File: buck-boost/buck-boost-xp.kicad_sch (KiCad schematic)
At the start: 0 parts

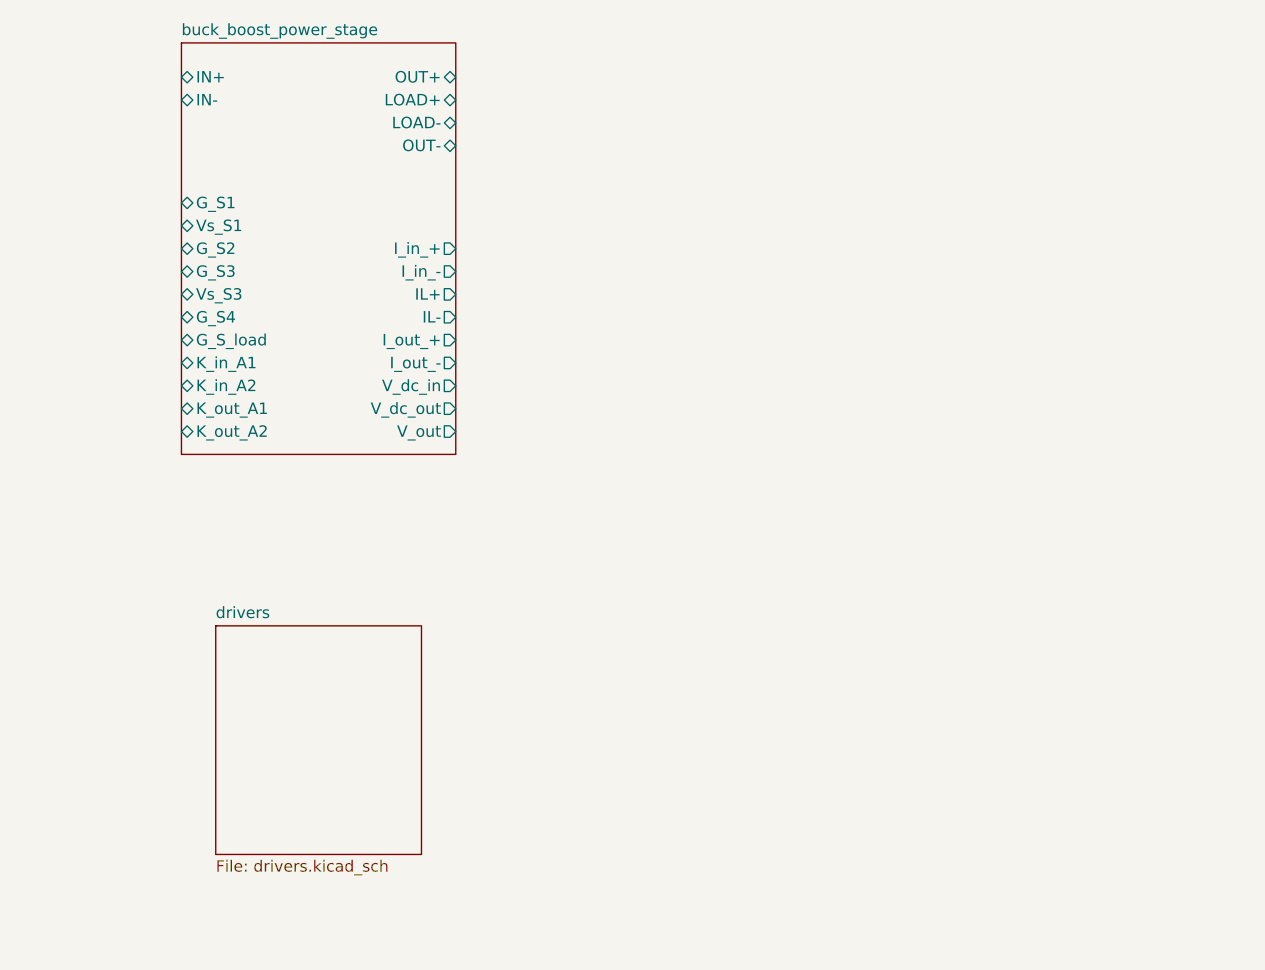
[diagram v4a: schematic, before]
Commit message: Adding connectors, test points to gate drivers
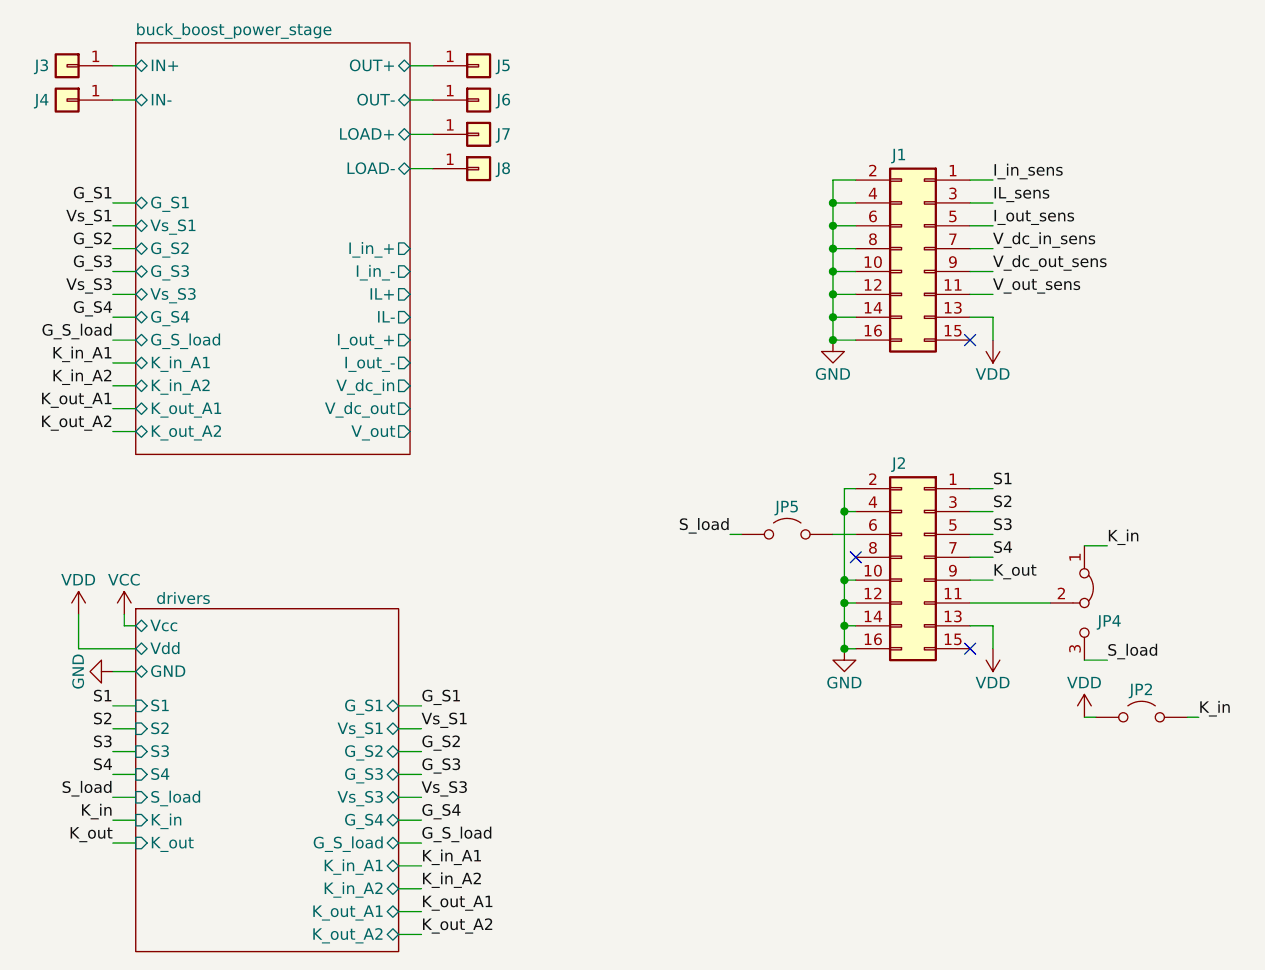
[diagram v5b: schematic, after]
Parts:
- added J1, J2: Conn_02x08_Odd_Even, Connector_PinHeader_2.54mm:PinHeader_2x08_P2.54mm_Horizontal, symbol Connector_Generic:Conn_02x08_Odd_Even
- added J3, J4, J5, J6, J7, J8: Conn_01x01, MountingHole:MountingHole_6.4mm_M6_Pad, symbol Connector_Generic:Conn_01x01
- added JP2, JP5: Jumper_2_Open, TestPoint:TestPoint_2Pads_Pitch2.54mm_Drill0.8mm, symbol Jumper:Jumper_2_Open
- added JP4: Jumper_3_Bridged12, Connector_PinHeader_2.54mm:PinHeader_1x03_P2.54mm_Vertical, symbol Jumper:Jumper_3_Bridged12
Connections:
- net buck_boost_power_stage/IN+: now also J3.1 (Pin_1)
- net buck_boost_power_stage/IN-: now also J4.1 (Pin_1)
- net buck_boost_power_stage/LOAD+: now also J7.1 (Pin_1)
- net buck_boost_power_stage/LOAD-: now also J8.1 (Pin_1)
- net buck_boost_power_stage/OUT+: now also J5.1 (Pin_1)
- net buck_boost_power_stage/OUT-: now also J6.1 (Pin_1)
- new net: J2.11 (Pin_11), JP4.2 (C)
- new net: J2.6 (Pin_6), JP5.2 (B)
- new net GND: J1.10 (Pin_10), J1.12 (Pin_12), J1.14 (Pin_14), J1.16 (Pin_16), J1.2 (Pin_2), J1.4 (Pin_4), J1.6 (Pin_6), J1.8 (Pin_8), J2.10 (Pin_10), J2.12 (Pin_12), J2.14 (Pin_14), J2.16 (Pin_16), J2.2 (Pin_2), J2.4 (Pin_4)
- new net IL_sens: J1.3 (Pin_3)
- new net I_in_sens: J1.1 (Pin_1)
- new net I_out_sens: J1.5 (Pin_5)
- new net K_in: JP2.2 (B), JP4.1 (A)
- new net K_out: J2.9 (Pin_9)
- new net S1: J2.1 (Pin_1)
- new net S2: J2.3 (Pin_3)
- new net S3: J2.5 (Pin_5)
- new net S4: J2.7 (Pin_7)
- new net S_load: JP4.3 (B), JP5.1 (A)
- new net VDD: J1.13 (Pin_13), J2.13 (Pin_13), JP2.1 (A)
- new net V_dc_in_sens: J1.7 (Pin_7)
- new net V_dc_out_sens: J1.9 (Pin_9)
- new net V_out_sens: J1.11 (Pin_11)
- no-connect marks 0 -> 3
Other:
- sheet drivers ports: added GND, G_S1, G_S2, G_S3, G_S4, G_S_load, K_in, K_in_A1, K_in_A2, K_out, K_out_A1, K_out_A2, S1, S2, S3, S4, S_load, Vcc, Vdd, Vs_S1, Vs_S3; removed none

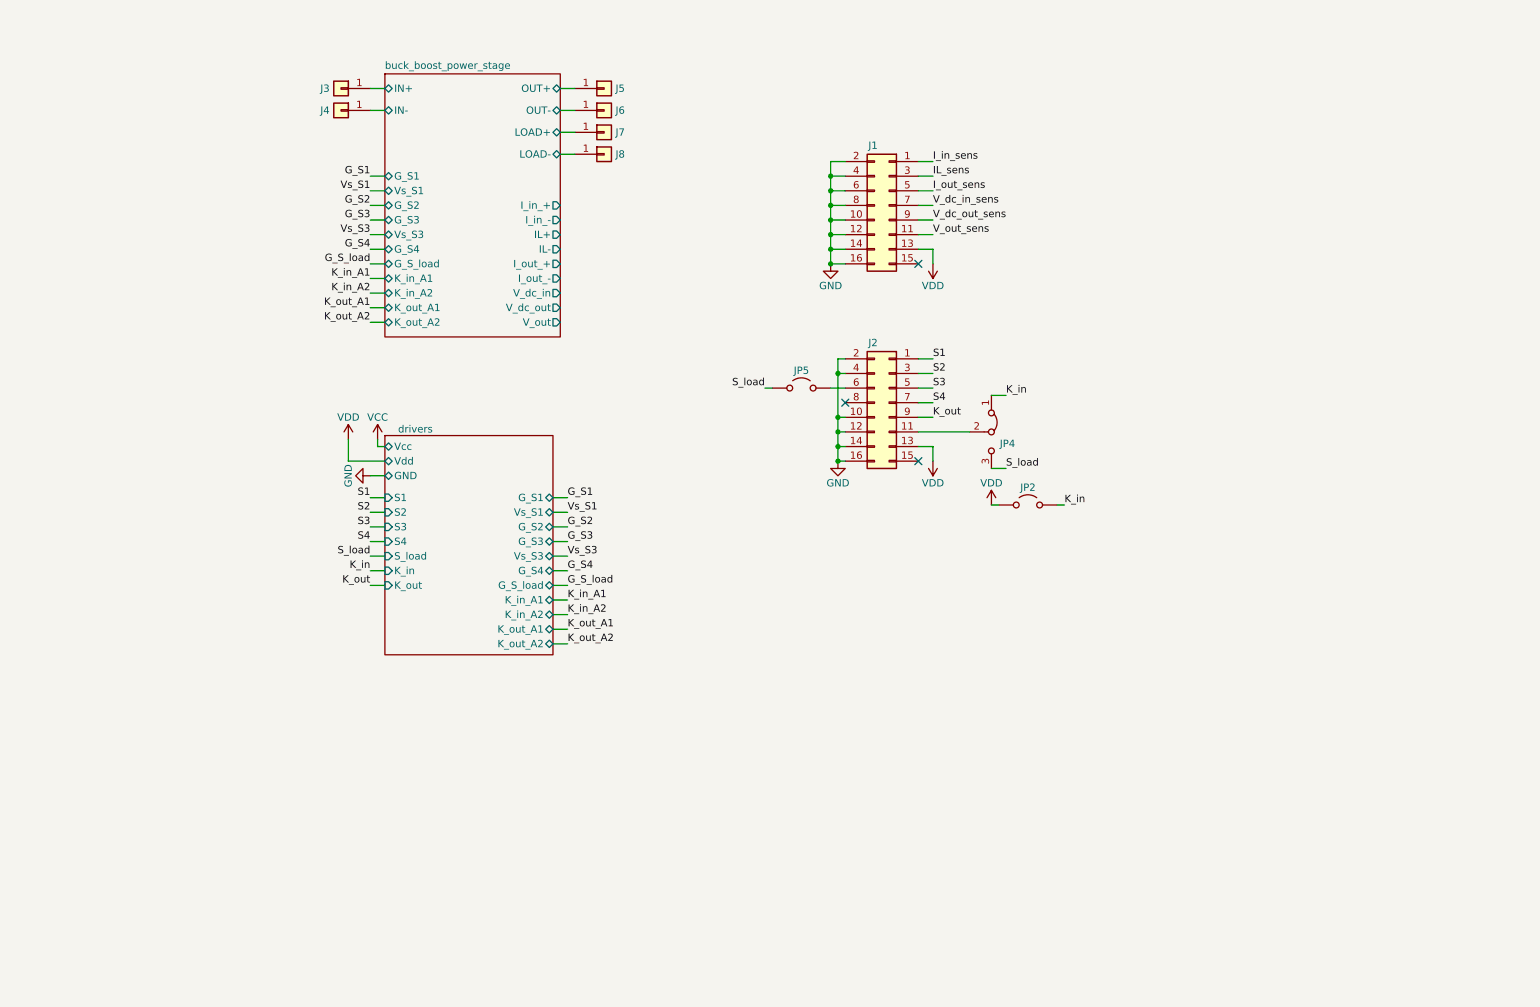
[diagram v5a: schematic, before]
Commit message: Adding current and voltage measurements blocks
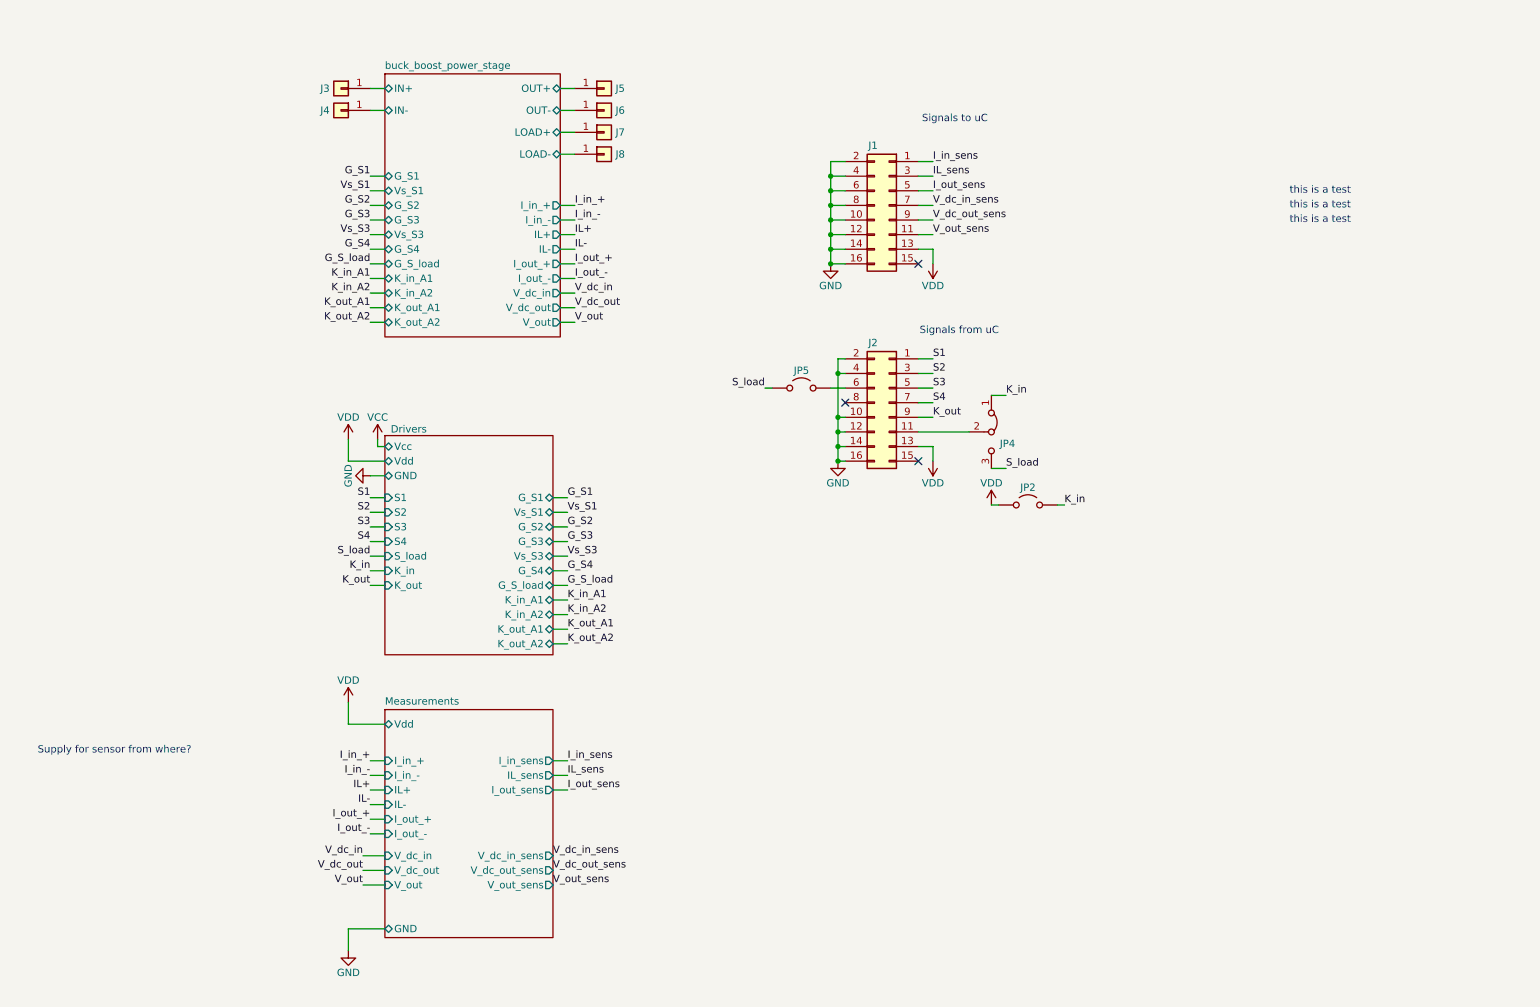
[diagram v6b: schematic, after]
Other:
- sheet drivers renamed Drivers
- added sheet Measurements (Measurements.kicad_sch)
- note added: "Signals from uC"
- note added: "Signals to uC"
- note added: "Supply for sensor from where?"
- note added: "this is a test"

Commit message: Editing sheets(Power labels, sheet color, adding text), Adding information in the sensor sheets
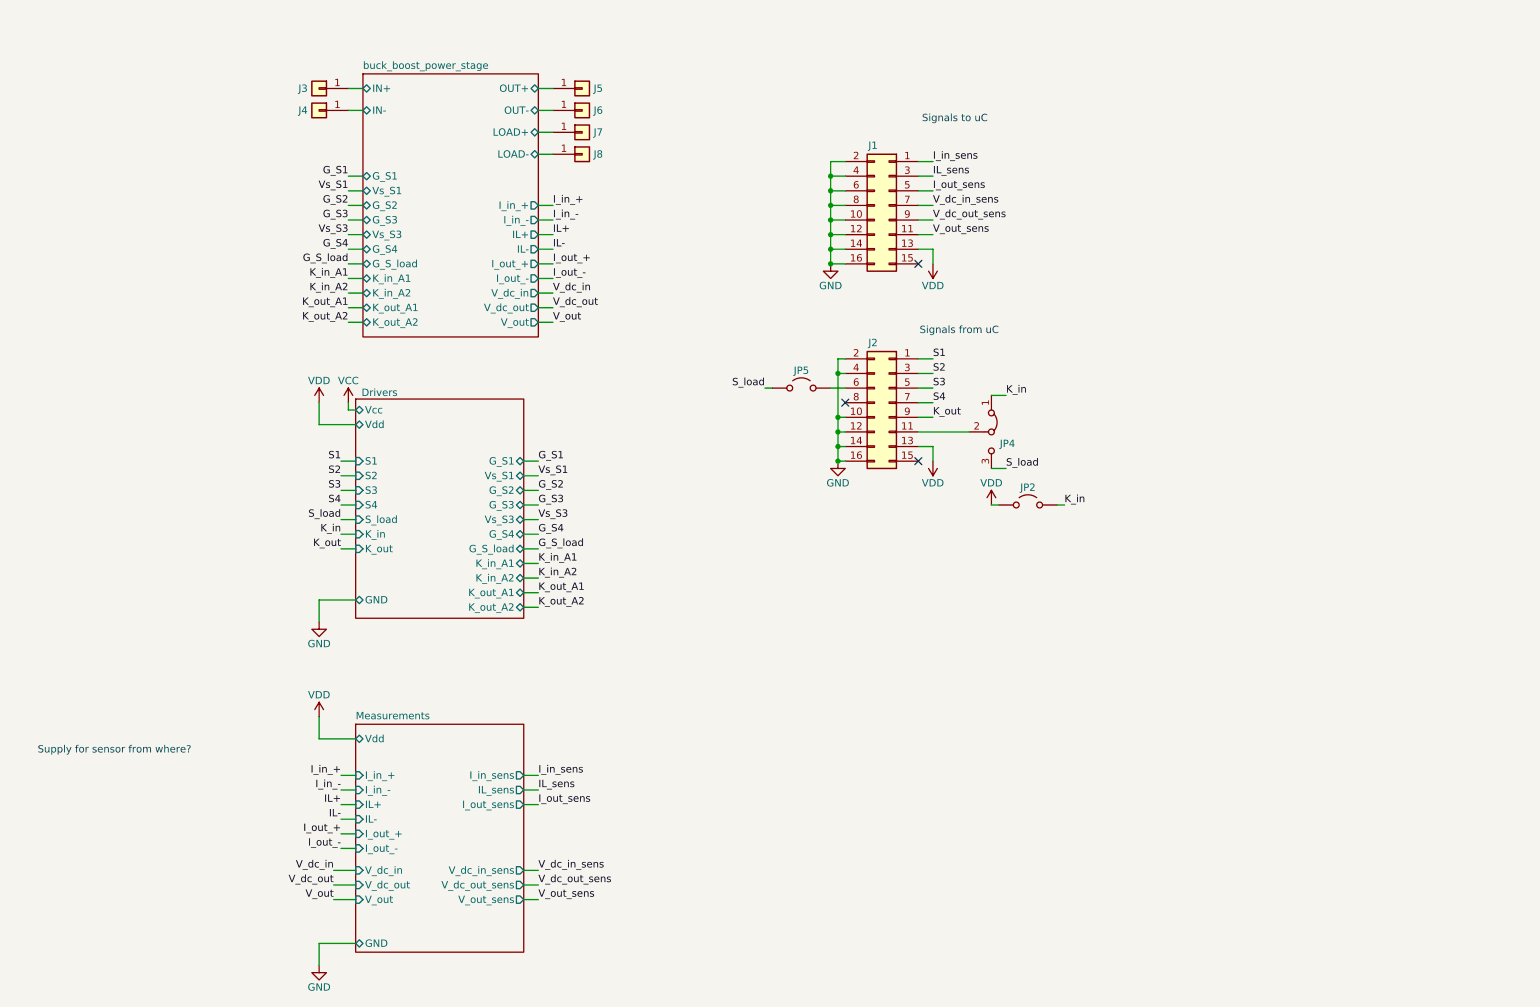
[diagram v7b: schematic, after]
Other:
- note removed: "this is a test"
- moved on the sheet: J3, J4, J5, J6, J7, J8

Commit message: Adding supply block
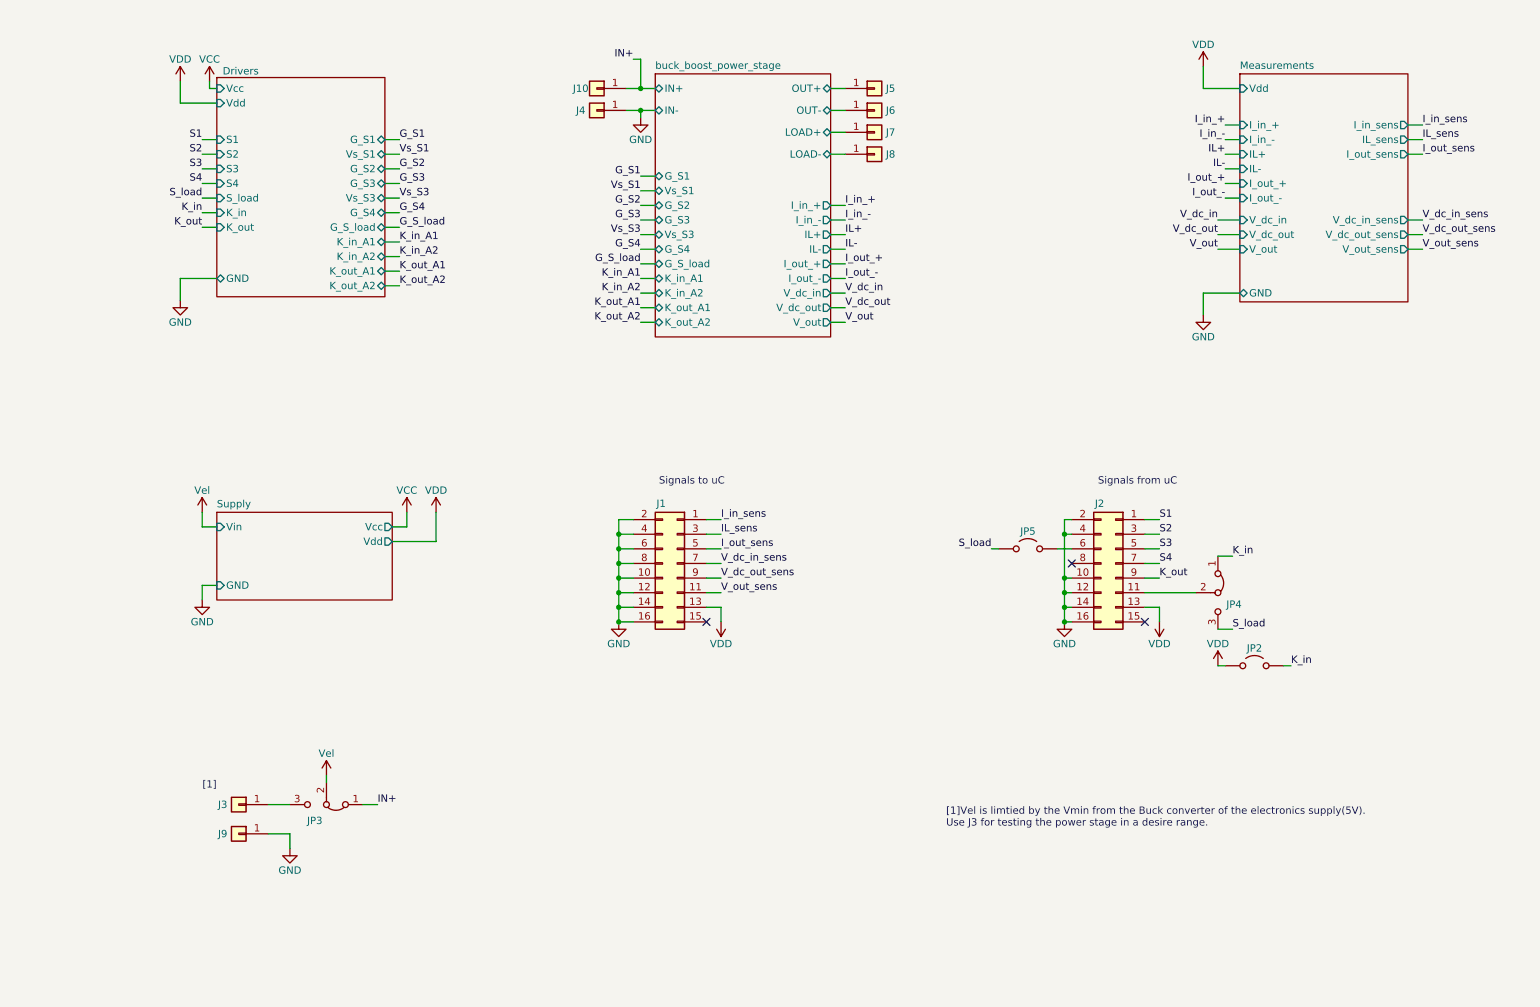
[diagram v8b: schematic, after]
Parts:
- added J10, J9: Conn_01x01, MountingHole:MountingHole_6.4mm_M6_Pad, symbol Connector_Generic:Conn_01x01
- added JP3: Jumper_3_Bridged12, Connector_PinHeader_2.54mm:PinHeader_1x03_P2.54mm_Vertical, symbol Jumper:Jumper_3_Bridged12
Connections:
- net buck_boost_power_stage/IN- is gone; now on net GND: J4.1 (Pin_1)
- net GND: now also J9.1 (Pin_1)
- net buck_boost_power_stage/IN+: no longer names the net of J3.1 (Pin_1)
- net buck_boost_power_stage/IN+: now also JP3.3 (B)
- new net IN+: J10.1 (Pin_1), JP3.1 (A)
- new net Vel: JP3.2 (C)
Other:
- added sheet Supply (buck-boost.kicad_sch)
- note added: "[1]"
- note added: "[1]Vel is limtied by the Vmin from the Buck converter of the electronics supply(5V). Use J3 for testing the power stage in a desire range."
- note removed: "Supply for sensor from where?"
- moved on the sheet: J1, J2, J3, J4, J5, J6, J7, J8, JP2, JP4, JP5
